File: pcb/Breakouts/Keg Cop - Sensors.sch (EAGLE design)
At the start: 6 parts

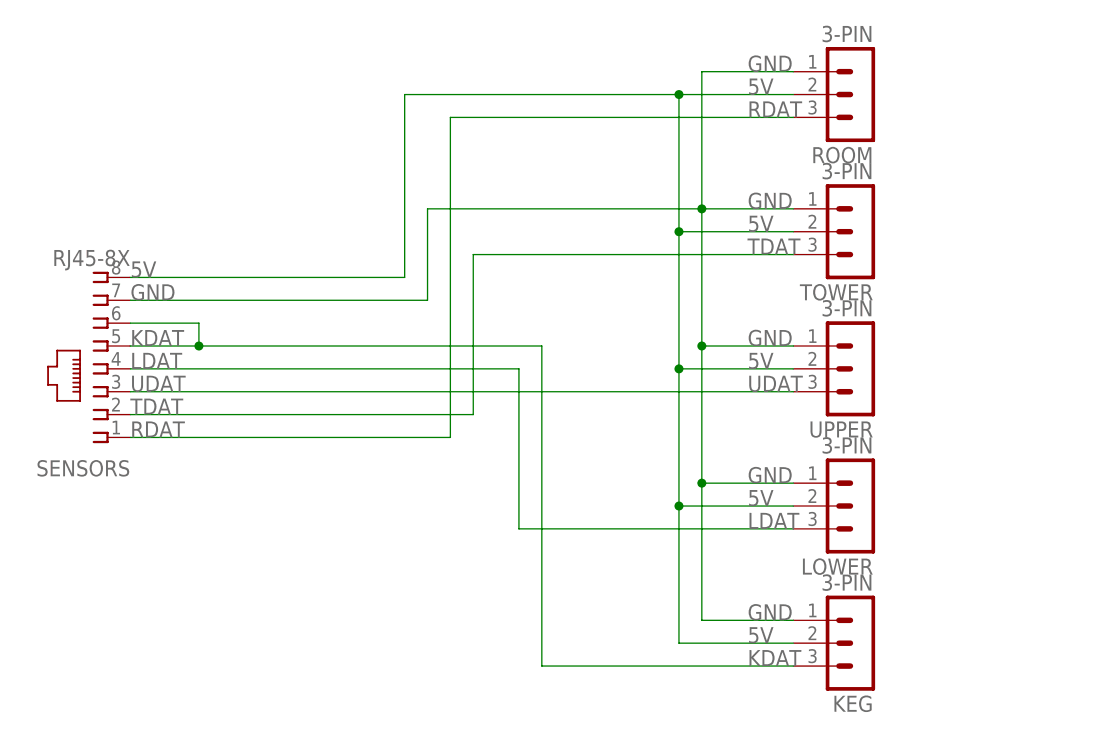
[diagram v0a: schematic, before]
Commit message: New sensor board
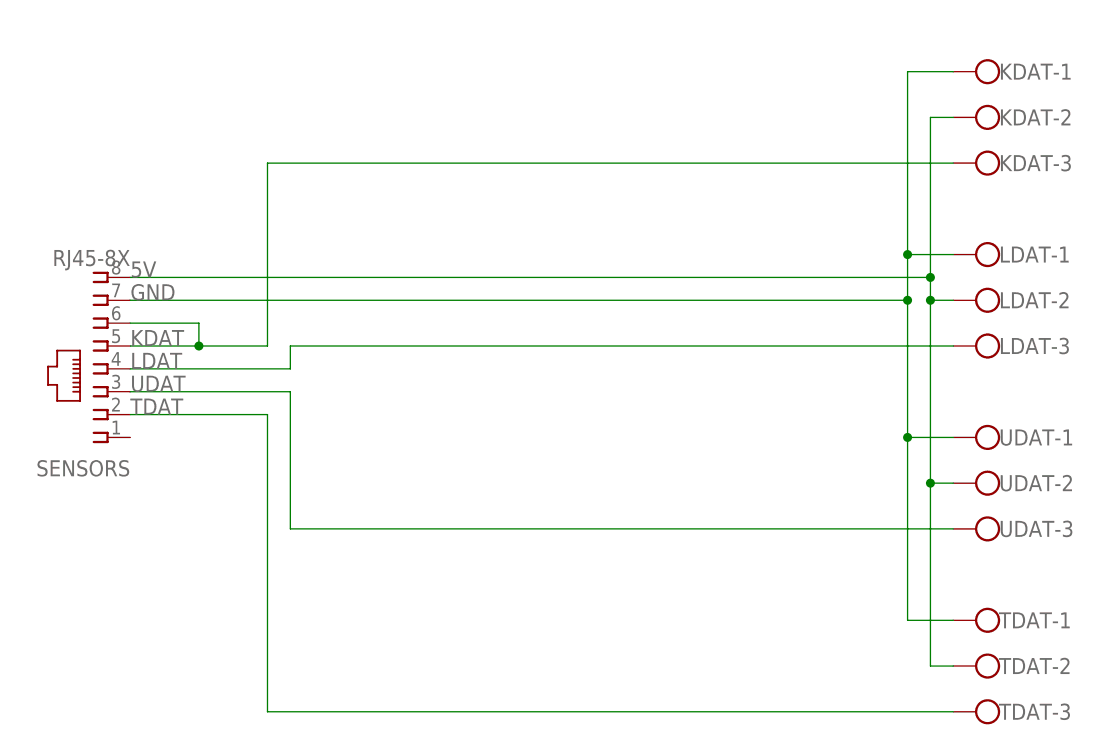
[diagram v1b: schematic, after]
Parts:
- removed KEG, LOWER, ROOM, TOWER, UPPER: 3-PIN, Donnie:HDR-3
- added KDAT, LDAT, TDAT, UDAT: (no value), con-wago-500:W237-103
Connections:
- removed net RDAT: ROOM.3, SENSORS.1
- net 5V: now also KDAT-2.KL, LDAT-2.KL, TDAT-2.KL, UDAT-2.KL; no longer KEG.2, LOWER.2, ROOM.2, TOWER.2, UPPER.2
- net GND: now also KDAT-1.KL, LDAT-1.KL, TDAT-1.KL, UDAT-1.KL; no longer KEG.1, LOWER.1, ROOM.1, TOWER.1, UPPER.1
- net KDAT: now also KDAT-3.KL; no longer KEG.3
- net LDAT: now also LDAT-3.KL; no longer LOWER.3
- net TDAT: now also TDAT-3.KL; no longer TOWER.3
- net UDAT: now also UDAT-3.KL; no longer UPPER.3
